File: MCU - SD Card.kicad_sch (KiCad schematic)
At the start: 8 parts

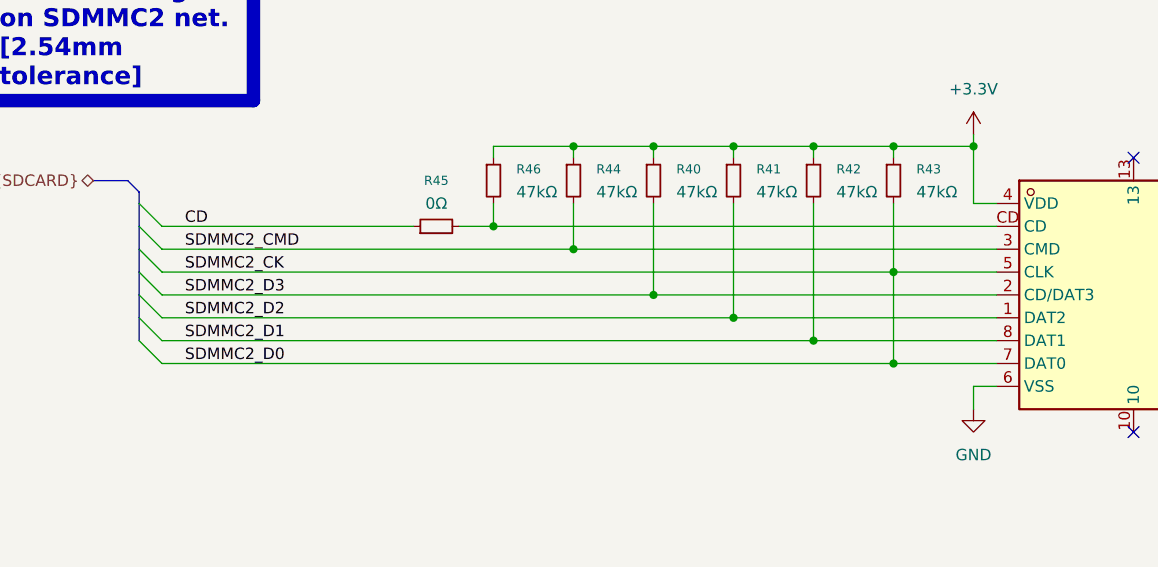
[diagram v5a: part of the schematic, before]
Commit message: duzo zmian, layout przetwornic i zasilania, wstepny routing sd card impedance control, usb differential impedance control
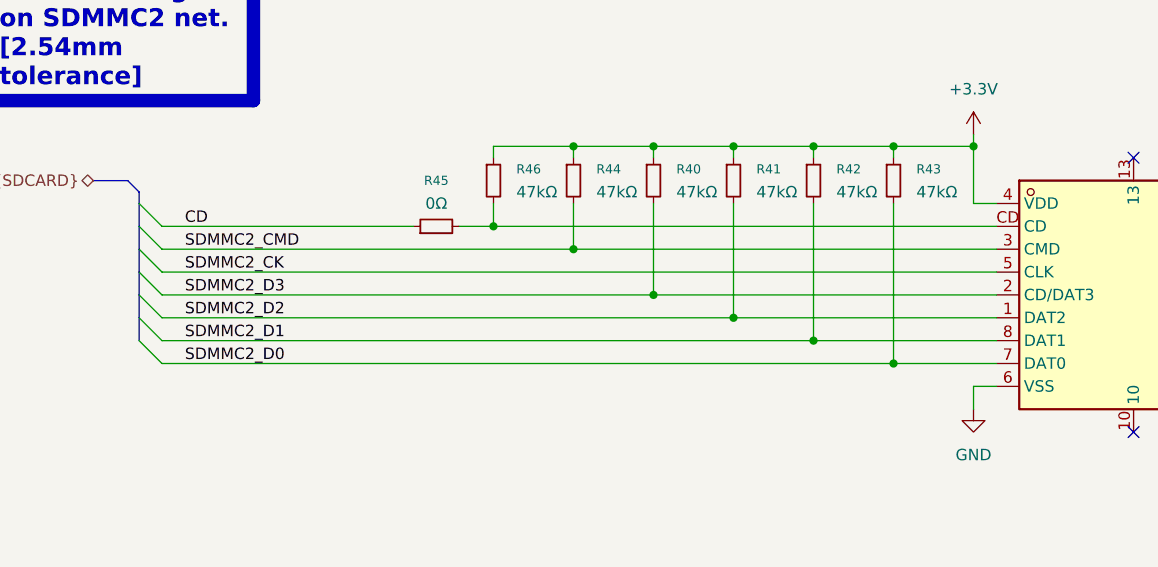
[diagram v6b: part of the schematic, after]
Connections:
- net SDMMC2_CK: no longer CARD1.7 (DAT0), R43.2
- new net SDMMC2_D0: CARD1.7 (DAT0), R43.2
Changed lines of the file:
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@@
-	)
-	(junction
-		(at 161.29 86.36)
-		(diameter 0)
-		(color 0 0 0 0)
 	)
 	(junction
@@
 	(wire
 		(pts
-			(xy 80.01 86.36) (xy 161.29 86.36)
+			(xy 80.01 86.36) (xy 172.72 86.36)
 		)
 		(stroke
@@
 	(wire
 		(pts
-			(xy 161.29 86.36) (xy 172.72 86.36)
-		)
-		(stroke
-			(width 0)
-			(type default)
-		)
-	)
-	(wire
-		(pts
 			(xy 170.18 78.74) (xy 172.72 78.74)
 		)
@@
 	(wire
 		(pts
-			(xy 161.29 78.74) (xy 161.29 86.36)
-		)
-		(stroke
-			(width 0)
-			(type default)
-		)
-	)
-	(wire
-		(pts
-			(xy 161.29 86.36) (xy 161.29 96.52)
-		)
-		(stroke
+			(xy 161.29 78.74) (xy 161.29 96.52)
+		)
+		(stroke
